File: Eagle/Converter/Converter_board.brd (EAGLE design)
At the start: 28.4 x 38.9 mm, 12 parts

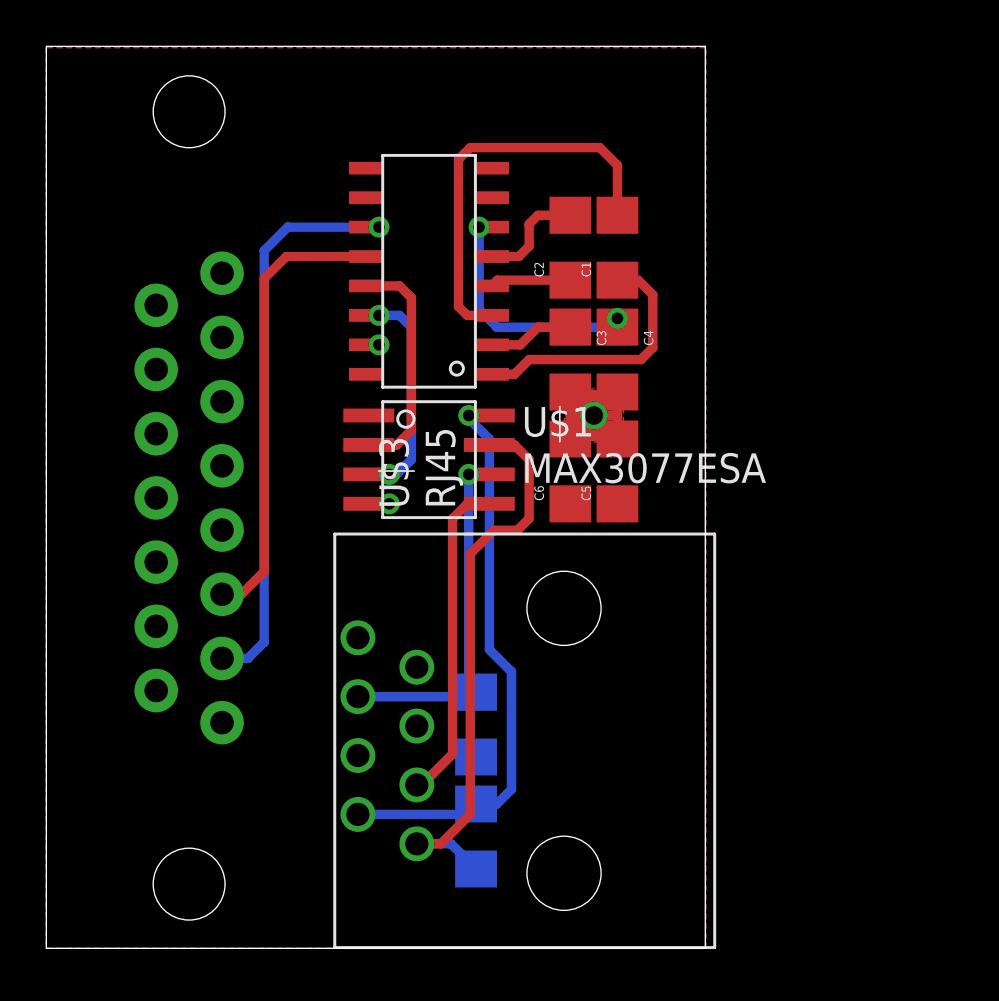
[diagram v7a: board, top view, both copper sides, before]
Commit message: Rotation RJ45
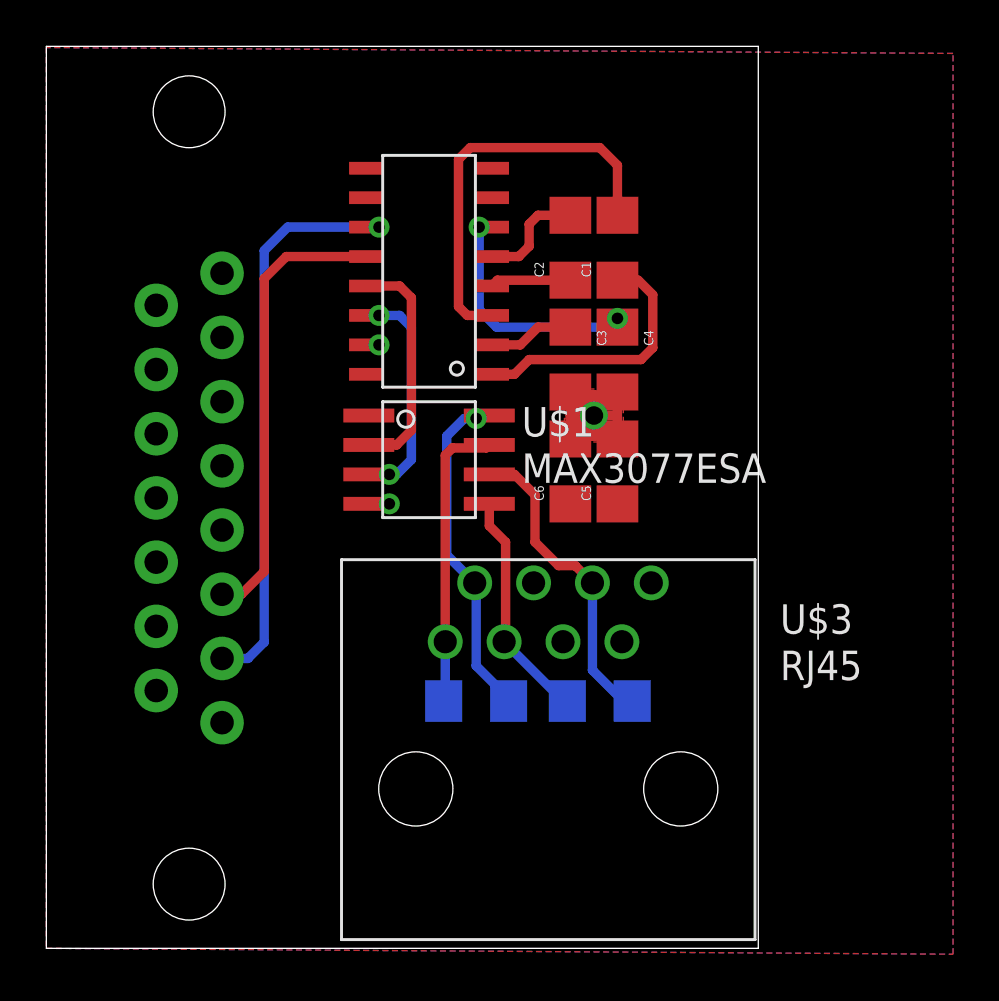
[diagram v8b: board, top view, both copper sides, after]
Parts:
- moved R1 5.84 mm to (18.5, 10.7), turned to 0 degrees
- moved R2 5.43 mm to (23.9, 10.7), turned to 0 degrees
- moved U$3 1.09 mm to (21.7, 8.57), turned to 0 degrees
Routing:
- net TRANS+: track 24.8 -> 13.7 mm
- net TRANS-: track 24.8 -> 14.7 mm
- net REC+: track 17.3 -> 11.0 mm
- net REC-: track 15.6 -> 14.6 mm, vias 1 -> 0
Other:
- board size 28.4 x 38.9 mm -> 30.7 x 38.9 mm
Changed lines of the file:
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@@
 <?xml version="1.0" encoding="utf-8"?>
 <!DOCTYPE eagle SYSTEM "eagle.dtd">
-<eagle version="6.5.0">
+<eagle version="6.6.0">
 <drawing>
 <settings>
@@
 <board>
 <plain>
-<wire x1="0" y1="0" x2="28.428" y2="0" width="0" layer="20"/>
-<wire x1="28.428" y1="0" x2="28.428" y2="38.913" width="0" layer="20"/>
-<wire x1="28.428" y1="38.913" x2="0" y2="38.913" width="0" layer="20"/>
+<wire x1="0" y1="0" x2="30.714" y2="0" width="0" layer="20"/>
+<wire x1="30.714" y1="0" x2="30.714" y2="38.913" width="0" layer="20"/>
+<wire x1="30.714" y1="38.913" x2="0" y2="38.913" width="0" layer="20"/>
 <wire x1="0" y1="38.913" x2="0" y2="0" width="0" layer="20"/>
 </plain>
@@
 <element name="C5" library="SparkFun-Capacitors" package="1206" value="0.1uF" x="24.638" y="20.574" rot="R90"/>
 <element name="C6" library="SparkFun-Capacitors" package="1206" value="0.1uF" x="22.606" y="20.574" rot="R90"/>
-<element name="U$3" library="MRDT-LIB2014" package="RJ45-CAT5E" value="RJ45" x="20.6375" y="8.9535" rot="R90"/>
+<element name="U$3" library="MRDT-LIB2014" package="RJ45-CAT5E" value="RJ45" x="21.6535" y="8.5725"/>
 <element name="U$4" library="MRDT-LIB2014" package="DB15" value="DB15" x="6.1595" y="19.431" rot="MR90"/>
-<element name="R1" library="SparkFun-Passives" package="1206" value="120" x="18.542" y="4.826" rot="MR270"/>
-<element name="R2" library="SparkFun-Passives" package="1206" value="120" x="18.542" y="9.652" rot="MR270"/>
+<element name="R1" library="SparkFun-Passives" package="1206" value="120" x="18.542" y="10.668" rot="MR0"/>
+<element name="R2" library="SparkFun-Passives" package="1206" value="120" x="23.876" y="10.668" rot="MR0"/>
 </elements>
 <signals>
@@
 <polygon width="0.4064" layer="16">
 <vertex x="0" y="0"/>
-<vertex x="28.448" y="0"/>
-<vertex x="28.448" y="38.862"/>
+<vertex x="39.116" y="-0.254"/>
+<vertex x="39.116" y="38.608"/>
 <vertex x="0" y="38.862"/>
 </polygon>
@@
 <polygon width="0.4064" layer="1">
 <vertex x="0" y="0"/>
-<vertex x="28.448" y="0"/>
-<vertex x="28.448" y="38.862"/>
+<vertex x="39.116" y="-0.254"/>
+<vertex x="39.116" y="38.608"/>
 <vertex x="0" y="38.862"/>
 </polygon>
@@
 <contactref element="R1" pad="2"/>
 <contactref element="U$1" pad="7"/>
-<wire x1="15.9825" y1="4.5085" x2="17.4595" y2="4.5085" width="0.4064" layer="16"/>
-<wire x1="17.4595" y1="4.5085" x2="18.542" y2="3.426" width="0.4064" layer="16"/>
-<wire x1="19.11" y1="21.717" x2="20.193" y2="21.717" width="0.4064" layer="1"/>
-<wire x1="20.193" y1="21.717" x2="20.828" y2="21.082" width="0.4064" layer="1"/>
-<wire x1="20.828" y1="21.082" x2="20.828" y2="18.542" width="0.4064" layer="1"/>
-<wire x1="20.828" y1="18.542" x2="20.32" y2="18.034" width="0.4064" layer="1"/>
-<wire x1="20.32" y1="18.034" x2="19.304" y2="18.034" width="0.4064" layer="1"/>
-<wire x1="19.304" y1="18.034" x2="18.288" y2="17.018" width="0.4064" layer="1"/>
-<wire x1="18.288" y1="17.018" x2="18.288" y2="5.7785" width="0.4064" layer="1"/>
-<wire x1="18.288" y1="5.7785" x2="17.018" y2="4.5085" width="0.4064" layer="1"/>
-<wire x1="17.018" y1="4.5085" x2="15.9825" y2="4.5085" width="0.4064" layer="1"/>
+<wire x1="17.142" y1="10.668" x2="17.2085" y2="10.16" width="0.4064" layer="16"/>
+<wire x1="17.2085" y1="13.2275" x2="17.2085" y2="21.2725" width="0.4064" layer="1"/>
+<wire x1="17.2085" y1="21.2725" x2="17.526" y2="21.59" width="0.4064" layer="1"/>
+<wire x1="17.526" y1="21.59" x2="18.983" y2="21.59" width="0.4064" layer="1"/>
+<wire x1="18.983" y1="21.59" x2="19.11" y2="21.717" width="0.4064" layer="1"/>
+<wire x1="17.2085" y1="10.16" x2="17.2085" y2="13.2275" width="0.4064" layer="16"/>
 </signal>
 <signal name="TRANS-">
@@
 <contactref element="R1" pad="1"/>
 <contactref element="U$1" pad="8"/>
-<wire x1="13.4425" y1="5.7785" x2="18.0945" y2="5.7785" width="0.4064" layer="16"/>
-<wire x1="18.0945" y1="5.7785" x2="18.542" y2="6.226" width="0.4064" layer="16"/>
-<wire x1="19.1135" y1="21.971" x2="18.2245" y2="22.86" width="0.4064" layer="16"/>
-<wire x1="18.2245" y1="22.86" x2="18.2245" y2="22.987" width="0.4064" layer="16"/>
-<via x="18.2245" y="22.987" extent="1-16" drill="0.5"/>
-<wire x1="18.2245" y1="22.987" x2="19.11" y2="22.987" width="0.4064" layer="1"/>
-<wire x1="18.542" y1="6.226" x2="19.434" y2="6.226" width="0.4064" layer="16"/>
-<wire x1="19.434" y1="6.226" x2="20.066" y2="6.858" width="0.4064" layer="16"/>
-<wire x1="20.066" y1="6.858" x2="20.066" y2="11.938" width="0.4064" layer="16"/>
-<wire x1="20.066" y1="11.938" x2="19.1135" y2="12.8905" width="0.4064" layer="16"/>
-<wire x1="19.1135" y1="12.8905" x2="19.1135" y2="21.971" width="0.4064" layer="16"/>
+<wire x1="19.942" y1="10.668" x2="19.942" y2="10.792" width="0.4064" layer="16"/>
+<wire x1="18.542" y1="12.192" x2="18.542" y2="15.704" width="0.4064" layer="16"/>
+<wire x1="18.542" y1="15.704" x2="18.4785" y2="15.7675" width="0.4064" layer="16"/>
+<wire x1="18.4785" y1="15.7675" x2="17.272" y2="16.974" width="0.4064" layer="16"/>
+<wire x1="17.272" y1="16.974" x2="17.272" y2="22.098" width="0.4064" layer="16"/>
+<wire x1="17.272" y1="22.098" x2="18.034" y2="22.86" width="0.4064" layer="16"/>
+<wire x1="18.034" y1="22.86" x2="18.542" y2="22.86" width="0.4064" layer="16"/>
+<via x="18.542" y="22.86" extent="1-16" drill="0.5"/>
+<wire x1="18.542" y1="22.86" x2="18.669" y2="22.987" width="0.4064" layer="1"/>
+<wire x1="18.669" y1="22.987" x2="19.11" y2="22.987" width="0.4064" layer="1"/>
+<wire x1="19.942" y1="10.792" x2="18.542" y2="12.192" width="0.4064" layer="16"/>
 </signal>
 <signal name="REC+">
@@
 <contactref element="R2" pad="2"/>
 <contactref element="U$1" pad="5"/>
-<wire x1="15.9825" y1="7.0485" x2="16.1925" y2="7.0485" width="0.4064" layer="1"/>
-<wire x1="16.1925" y1="7.0485" x2="17.526" y2="8.382" width="0.4064" layer="1"/>
-<wire x1="17.526" y1="8.382" x2="17.526" y2="18.542" width="0.4064" layer="1"/>
-<wire x1="17.526" y1="18.542" x2="18.161" y2="19.177" width="0.4064" layer="1"/>
-<wire x1="18.161" y1="19.177" x2="19.11" y2="19.177" width="0.4064" layer="1"/>
-<wire x1="18.542" y1="8.252" x2="18.412" y2="8.382" width="0.4064" layer="16"/>
-<wire x1="18.412" y1="8.382" x2="17.526" y2="8.382" width="0.4064" layer="16"/>
-<wire x1="17.526" y1="8.382" x2="16.1925" y2="7.0485" width="0.4064" layer="16"/>
-<wire x1="16.1925" y1="7.0485" x2="15.9825" y2="7.0485" width="0.4064" layer="16"/>
+<wire x1="22.476" y1="10.668" x2="22.73" y2="10.246" width="0.4064" layer="16"/>
+<wire x1="19.11" y1="19.177" x2="19.11" y2="18.228" width="0.4064" layer="1"/>
+<wire x1="19.11" y1="18.228" x2="19.812" y2="17.526" width="0.4064" layer="1"/>
+<wire x1="19.812" y1="17.526" x2="19.812" y2="13.291" width="0.4064" layer="1"/>
+<wire x1="19.812" y1="13.291" x2="19.7485" y2="13.2275" width="0.4064" layer="1"/>
+<wire x1="22.73" y1="10.246" x2="19.7485" y2="13.2275" width="0.4064" layer="16"/>
 </signal>
 <signal name="REC-">
@@
 <contactref element="R2" pad="1"/>
 <contactref element="U$1" pad="6"/>
-<wire x1="13.4425" y1="10.8585" x2="18.3485" y2="10.8585" width="0.4064" layer="16"/>
-<wire x1="18.3485" y1="10.8585" x2="18.542" y2="11.052" width="0.4064" layer="16"/>
-<wire x1="18.542" y1="11.052" x2="18.2245" y2="11.3695" width="0.4064" layer="16"/>
-<wire x1="18.2245" y1="11.3695" x2="18.2245" y2="20.447" width="0.4064" layer="16"/>
-<via x="18.2245" y="20.447" extent="1-16" drill="0.5"/>
-<wire x1="18.2245" y1="20.447" x2="19.11" y2="20.447" width="0.4064" layer="1"/>
+<wire x1="25.276" y1="10.668" x2="25.4" y2="10.16" width="0.4064" layer="16"/>
+<wire x1="23.622" y1="15.704" x2="23.5585" y2="15.7675" width="0.4064" layer="16"/>
+<wire x1="25.4" y1="10.16" x2="23.5585" y2="12.0015" width="0.4064" layer="16"/>
+<wire x1="23.5585" y1="12.0015" x2="23.5585" y2="15.7675" width="0.4064" layer="16"/>
+<wire x1="23.5585" y1="15.7675" x2="22.816" y2="16.51" width="0.4064" layer="1"/>
+<wire x1="22.816" y1="16.51" x2="22.098" y2="16.51" width="0.4064" layer="1"/>
+<wire x1="22.098" y1="16.51" x2="21.082" y2="17.526" width="0.4064" layer="1"/>
+<wire x1="21.082" y1="17.526" x2="21.082" y2="19.558" width="0.4064" layer="1"/>
+<wire x1="21.082" y1="19.558" x2="20.193" y2="20.447" width="0.4064" layer="1"/>
+<wire x1="20.193" y1="20.447" x2="19.11" y2="20.447" width="0.4064" layer="1"/>
 </signal>
 <signal name="T_IN1">
